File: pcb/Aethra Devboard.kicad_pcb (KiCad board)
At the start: 2 copper layers, 21 x 51 mm, 44 parts, among them J1 USB_C_Receptacle_USB2.0_14P, J2 Conn_01x20, J3 Conn_01x20, J4 Conn_01x03, J5 Conn_01x02, Q1 DMG2301L, SW1 SW_Push, U1 RP2040, U2 AP2112K-3.3, U3 W25Q16JVZPIQ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

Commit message: Finish routing PCB
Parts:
- moved C17 122.5 mm to (153.2, 98.4), turned to 90 degrees
- moved C18 117.9 mm to (156.6, 86.0), turned to 90 degrees
- moved R1 112.3 mm to (152.4, 87.2), turned to 90 degrees
- moved R7 107.6 mm to (145.6, 98.3), turned to -90 degrees
- moved R2 107.5 mm to (148.4, 86.4), turned to 180 degrees
- moved R9 106.0 mm to (148.5, 91.7), turned to 180 degrees
- moved R8 100.8 mm to (144.7, 85.0), turned to 90 degrees
- moved D3 71.3 mm to (155.8, 98.6), turned to -90 degrees
- moved C16 70.5 mm to (156.2, 115.0), turned to 90 degrees
- moved C14 69.3 mm to (150.6, 91.7), turned to 0 degrees
- moved U2 68.3 mm to (148.6, 89.1)
- moved C7 67.1 mm to (145.4, 110.2), turned to 0 degrees
- moved C5 66.9 mm to (156.8, 108.6)
- moved R6 66.9 mm to (146.6, 98.3)
- moved Q1 66.4 mm to (155.0, 87.8)
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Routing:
- net GND: track 0.00 -> 127.6 mm, vias 0 -> 21
- net +3V3: track 17.7 -> 95.6 mm, vias 2 -> 10
- net VBUS: track 1.39 -> 71.4 mm, vias 0 -> 3
- net +BATT: track 6.89 -> 46.2 mm, vias 0 -> 2
- net GPIO0: track 0.00 -> 30.5 mm, vias 0 -> 1
- net GPIO1: track 0.00 -> 27.7 mm, vias 0 -> 1
- net GPIO29_ADC3: track 0.00 -> 27.6 mm, vias 0 -> 2
- net GPIO28_ADC2: track 0.00 -> 23.7 mm, vias 0 -> 2
- net GPIO2: track 0.00 -> 22.9 mm
- net GPIO16: track 0.00 -> 22.7 mm, vias 0 -> 1
- net GPIO3: track 0.00 -> 20.8 mm
- net GPIO17: track 0.00 -> 19.0 mm, vias 0 -> 1
- net RUN: track 12.7 -> 31.4 mm, vias 1 -> 3
- net GPIO4: track 0.00 -> 18.6 mm
- net GPIO27_ADC1: track 0.00 -> 18.3 mm
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- added copper zone on B.Cu, net GND
- added copper zone on F.Cu, net GND

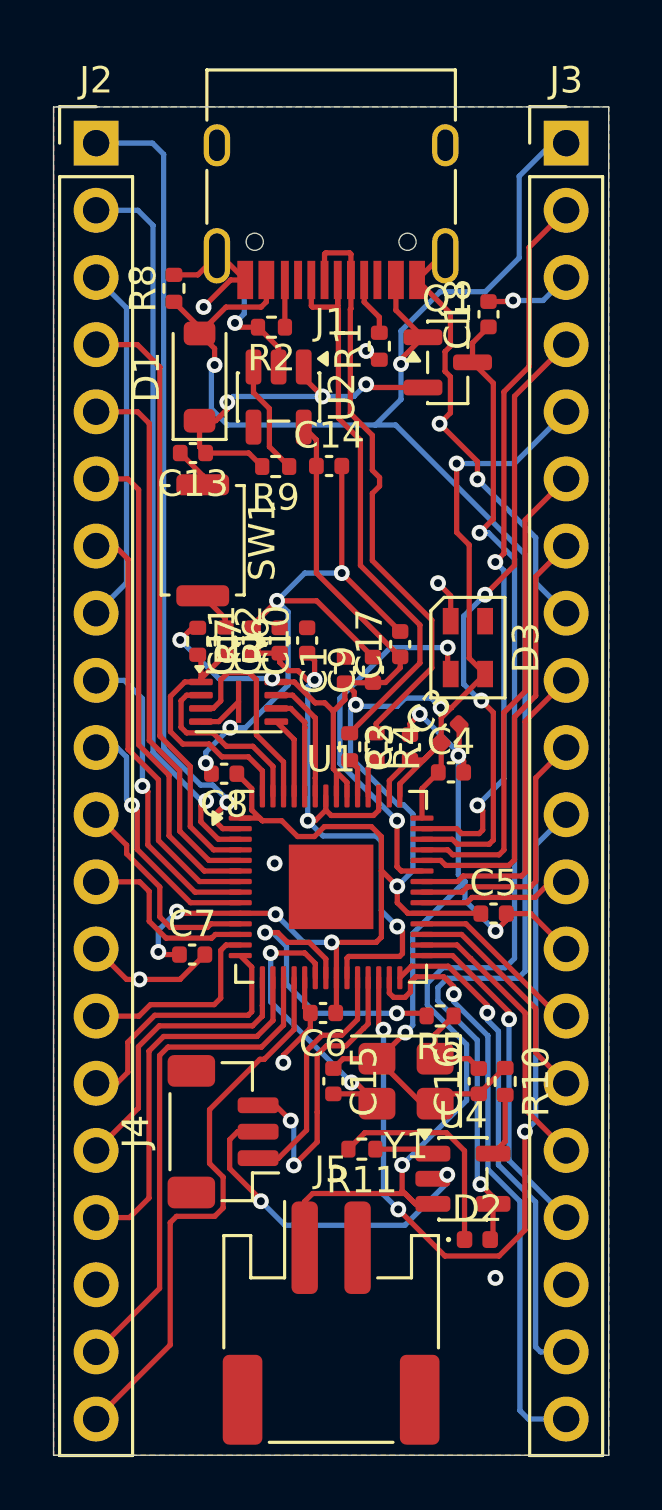
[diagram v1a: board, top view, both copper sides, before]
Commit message: Add 3d models to viewer
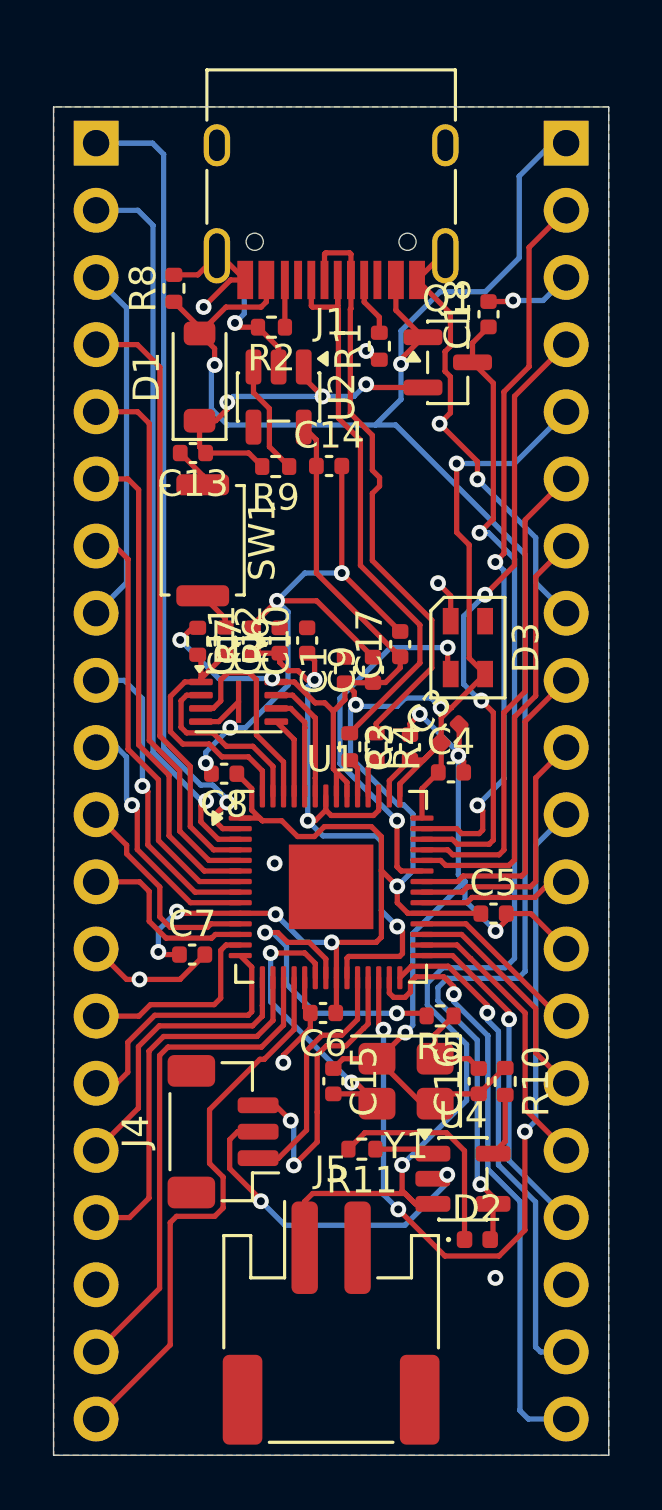
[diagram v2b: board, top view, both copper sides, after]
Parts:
- J2, J3: moved to B.Cu
- turned J2 to 180 degrees
- turned J3 to 180 degrees

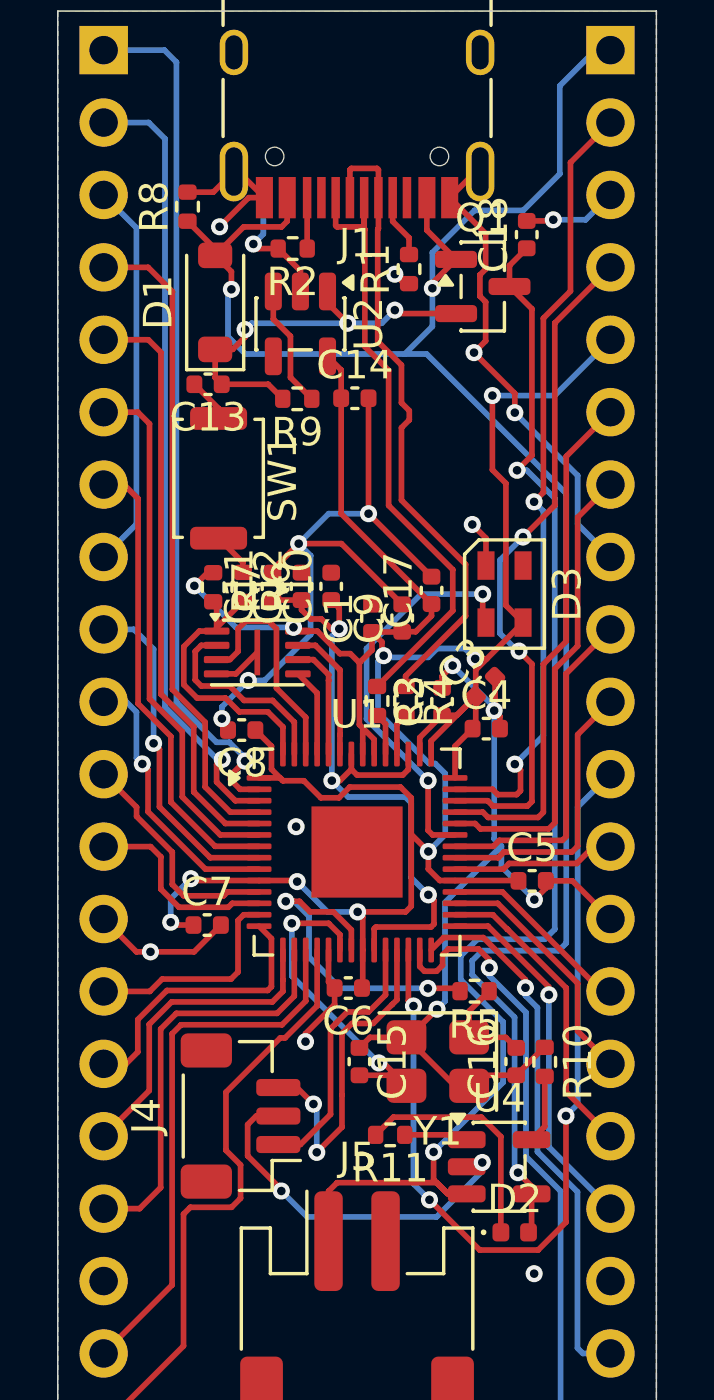
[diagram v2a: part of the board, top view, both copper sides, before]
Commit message: Add pinouts and icon to silkscreen
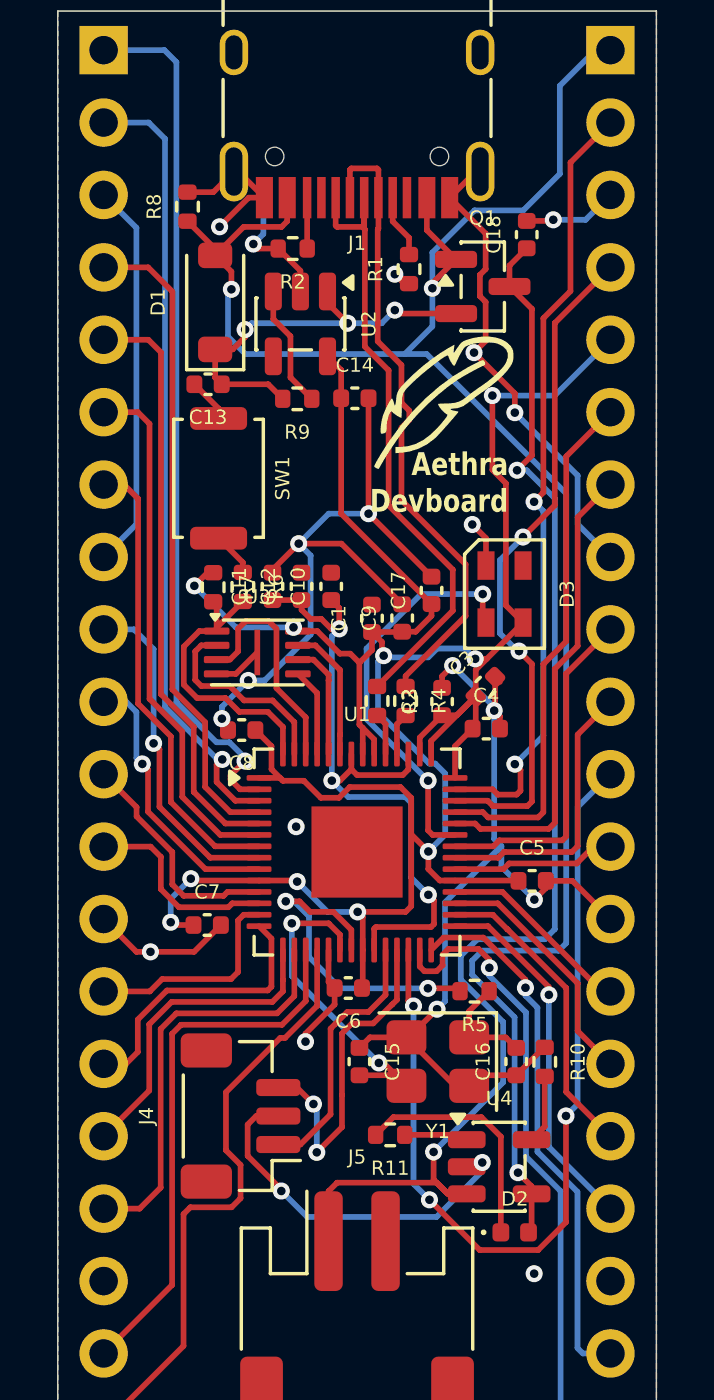
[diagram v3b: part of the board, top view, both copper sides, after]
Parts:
- added G***: ICON, ICON:icon, F.Cu at (153.5, 91.8)
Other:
- board text added: "3V3"
- board text added: "Aethra Devboard"
- board text added: "GND"
- board text added: "GPIO0"
- board text added: "GPIO1"
- board text added: "GPIO10"
- board text added: "GPIO11"
- board text added: "GPIO12"
- board text added: "GPIO13"
- board text added: "GPIO14"
- board text added: "GPIO15"
- board text added: "GPIO16"
- board text added: "GPIO17"
- board text added: "GPIO18"
- board text added: "GPIO19"
- board text added: "GPIO2"
- board text added: "GPIO20"
- board text added: "GPIO21"
- board text added: "GPIO22"
- board text added: "GPIO23"
- board text added: "GPIO24"
- board text added: "GPIO26_ADC0"
- board text added: "GPIO27_ADC1"
- board text added: "GPIO28_ADC2"
- board text added: "GPIO29_ADC3"
- board text added: "GPIO3"
- board text added: "GPIO4"
- board text added: "GPIO5"
- board text added: "GPIO6"
- board text added: "GPIO7"
- board text added: "GPIO8"
- board text added: "GPIO9"
- board text added: "RUN"
- board text added: "VBUS"

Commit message: Reroute PCB
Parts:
- moved C18 33.3 mm to (149.6, 118.5), turned to 0 degrees
- moved C12 14.1 mm to (153.6, 111.5), turned to -90 degrees
- moved C9 12.1 mm to (152.5, 111.5), turned to -90 degrees
- moved D2 12.1 mm to (144.6, 117.4), turned to 90 degrees
- moved R10 10.8 mm to (146.4, 115.6), turned to 180 degrees
- moved U4 8.76 mm to (146.9, 118.2), turned to 90 degrees
- moved J4 8.76 mm to (155.3, 117.4), turned to -90 degrees
- moved Q1 8.39 mm to (147.0, 90.3), turned to -90 degrees
- moved C7 7.95 mm to (145.9, 102.2), turned to 180 degrees
- moved C6 7.64 mm to (155.8, 107.0), turned to 0 degrees
- moved R11 7.41 mm to (144.6, 119.3), turned to 90 degrees
- moved R8 6.25 mm to (149.6, 88.8), turned to 0 degrees
- moved C5 6.15 mm to (155.8, 102.5)
- moved C11 6.11 mm to (153.3, 100.5)
- moved U2 5.98 mm to (146.6, 94.7), turned to 0 degrees
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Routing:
- net GND: track 127.6 -> 97.0 mm, vias 21 -> 16
- net RUN: track 31.4 -> 10.1 mm, vias 3 -> 1
- net +3V3: track 95.6 -> 74.9 mm, vias 10 -> 4
- net +1V1: track 24.2 -> 37.6 mm
- net +BATT: track 46.2 -> 33.5 mm
- net VBUS: track 71.4 -> 60.1 mm, vias 3 -> 2
- net XOUT: track 11.7 -> 1.83 mm, vias 2 -> 0
- net Net-(D2-K): track 8.29 -> 0.95 mm
- net Net-(D1-K): track 14.3 -> 8.83 mm, vias 3 -> 0
- net SWCLK: track 9.27 -> 13.7 mm, vias 0 -> 2
- net GPIO21: track 6.90 -> 11.3 mm, vias 0 -> 2
- net XIN: track 11.7 -> 7.49 mm, vias 2 -> 0
- net NEOPIXEL: track 14.2 -> 10.1 mm
- net GPIO0: track 30.5 -> 26.8 mm
- net QSPI_SS: track 10.3 -> 12.9 mm
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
